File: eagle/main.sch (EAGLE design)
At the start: 32 parts, among them IC1 7805TV, U1 INA213AIDCKT, U2 LM1117MP-3.3, U3 INA213AIDCKT, U4 INA213AIDCKT, U5 S25FL064K0SMFI011

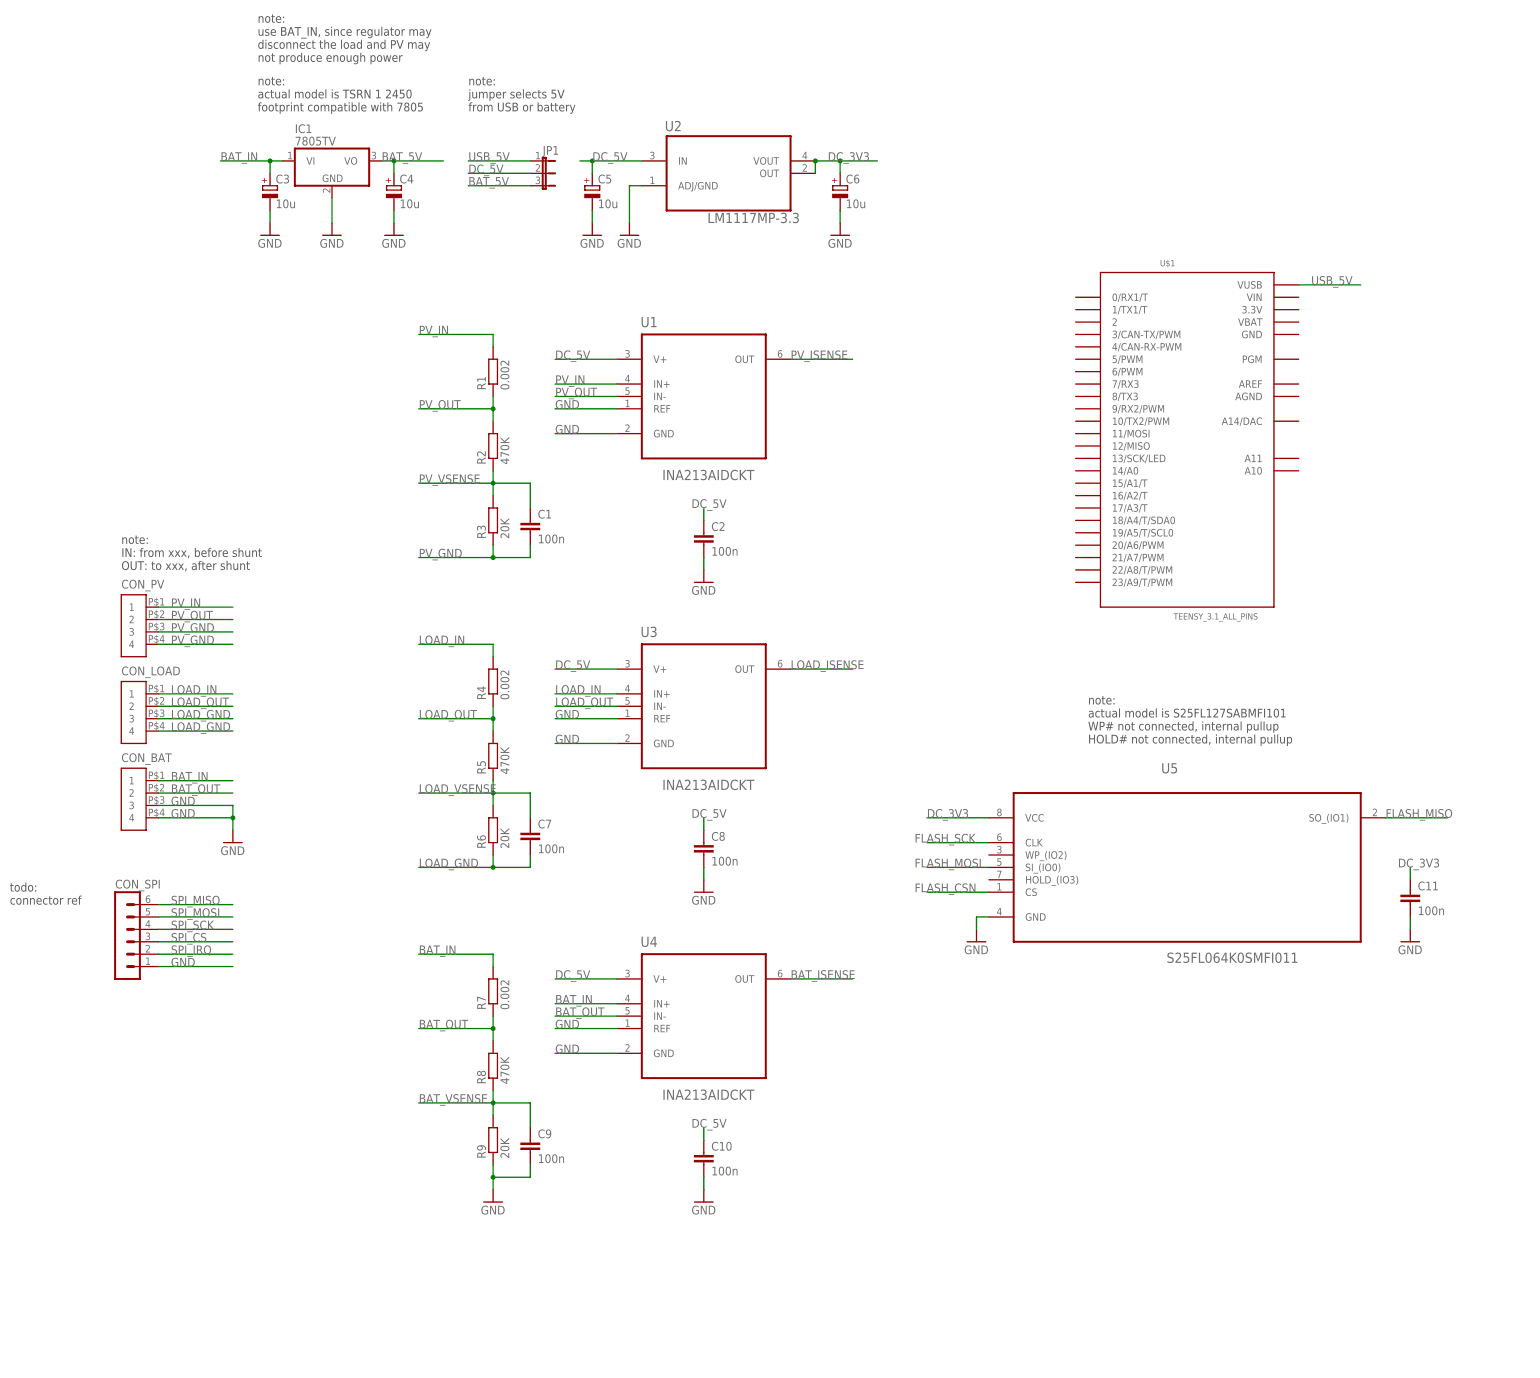
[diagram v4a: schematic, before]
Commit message: add TI library
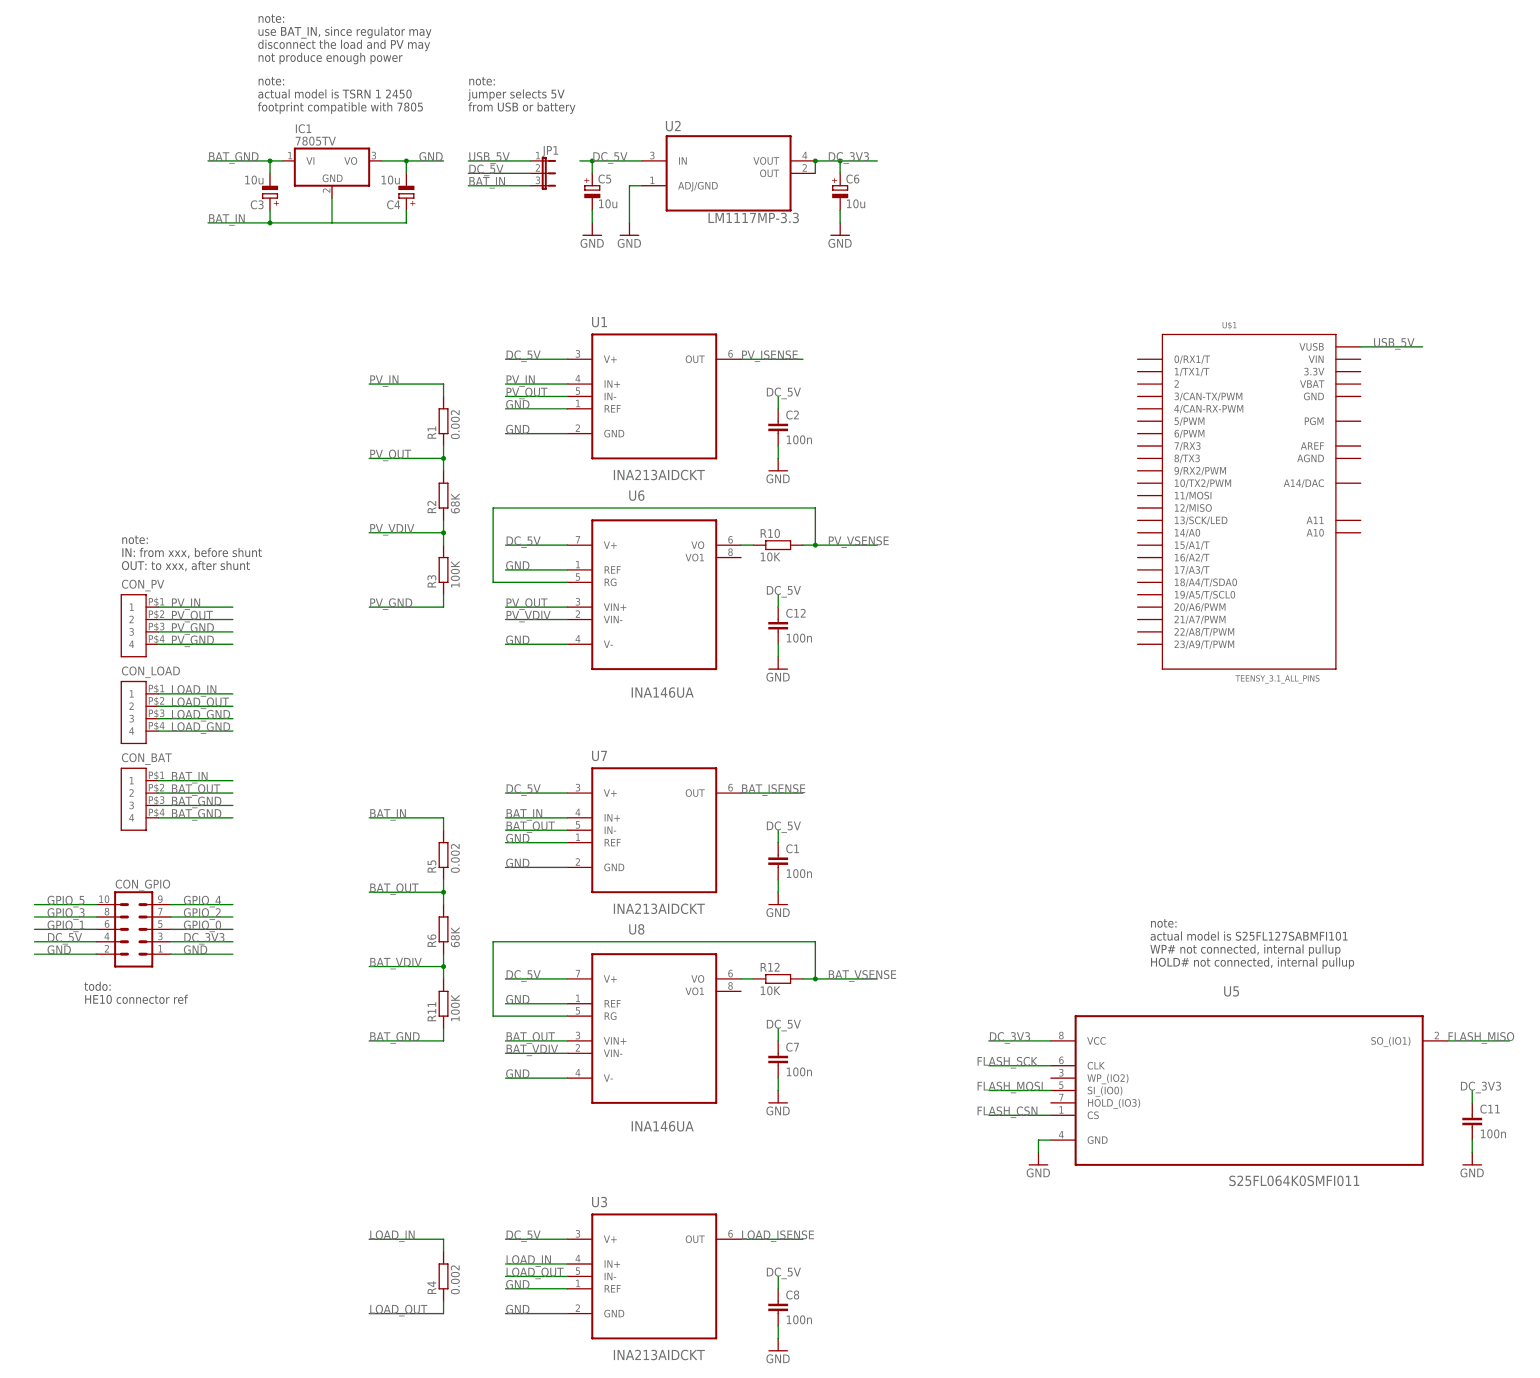
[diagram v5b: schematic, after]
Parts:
- removed C10, C9: 100n, rcl:C-EUC1206
- removed CON_SPI: (no value), con-lstb:MA06-1
- removed R7: 0.002, resistor:R-EU_R2512
- removed R8: 470K, rcl:R-EU_R0603
- removed R9: 20K, rcl:R-EU_R0603
- removed U4: INA213AIDCKT, TI-INA213AIDCKT:INA213AIDCKT
- added C12: 100n, rcl:C-EUC1206
- added CON_GPIO: (no value), con-lstb:MA05-2
- added R10, R12: 10K, rcl:R-EU_R0603
- added R11: 100K, rcl:R-EU_R0603
- added U6, U8: INA146UA, Texas Instruments_By_element14_Batch_1:INA146UA
- added U7: INA213AIDCKT, TI-INA213AIDCKT:INA213AIDCKT
- R2: value 470K -> 68K
- R3: value 20K -> 100K
- R5: value 470K -> 0.002; device rcl:R-EU_R0603 -> resistor:R-EU_R2512
- R6: value 20K -> 68K
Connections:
- removed net BAT_5V: C4.+, IC1.VO, JP1.3
- removed net LOAD_VSENSE: C7.1, R5.1, R6.2
- removed net SPI_CS: CON_SPI.3
- removed net SPI_IRQ: CON_SPI.2
- removed net SPI_MISO: CON_SPI.6
- removed net SPI_MOSI: CON_SPI.5
- removed net SPI_SCK: CON_SPI.4
- new net BAT_GND: C3.-, CON_BAT.3, CON_BAT.4, IC1.VI, R11.1
- new net BAT_VDIV: R11.2, R6.1, U8.VIN-
- new net GPIO_0: CON_GPIO.5
- new net GPIO_1: CON_GPIO.6
- new net GPIO_2: CON_GPIO.7
- new net GPIO_3: CON_GPIO.8
- new net GPIO_4: CON_GPIO.9
- new net GPIO_5: CON_GPIO.10
- new net N$1: R12.1, U8.VO
- new net N$2: R10.1, U6.VO
- new net N$4: IC1.GND
- new net PV_VDIV: R2.1, R3.2, U6.VIN-
- net BAT_IN: now also C4.+, JP1.3, R5.2, U7.IN+; no longer IC1.VI, R7.2, U4.IN+
- net BAT_ISENSE: now also U7.OUT; no longer U4.OUT
- net BAT_OUT: now also R5.1, R6.2, U7.IN-, U8.VIN+; no longer R7.1, R8.2, U4.IN-
- net BAT_VSENSE: now also R12.2, U8.RG; no longer C9.1, R8.1, R9.2
- net DC_3V3: now also CON_GPIO.3
- net DC_5V: now also C1.1, C12.1, C7.1, CON_GPIO.4, U6.V+, U7.V+, U8.V+; no longer C10.1, U4.V+
- net GND: now also C1.2, C12.2, C7.2, CON_GPIO.1, CON_GPIO.2, IC1.VO, U6.REF, U6.V-, U7.GND, U7.REF, U8.REF, U8.V-; no longer C10.2, C3.-, C9.2, CON_BAT.3, CON_BAT.4, CON_SPI.1, IC1.GND, R9.1, U4.GND, U4.REF
- net LOAD_GND: no longer C7.2, R6.1
- net LOAD_OUT: no longer R5.2
- net PV_GND: no longer C1.2
- net PV_OUT: now also U6.VIN+
- net PV_VSENSE: now also R10.2, U6.RG; no longer C1.1, R2.1, R3.2
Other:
- note added: "todo: HE10 connector ref"
- note removed: "todo: connector ref"
- moved on the sheet: C1, C11, C2, C3, C4, C7, C8, R1, R2, R3, R4, R5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

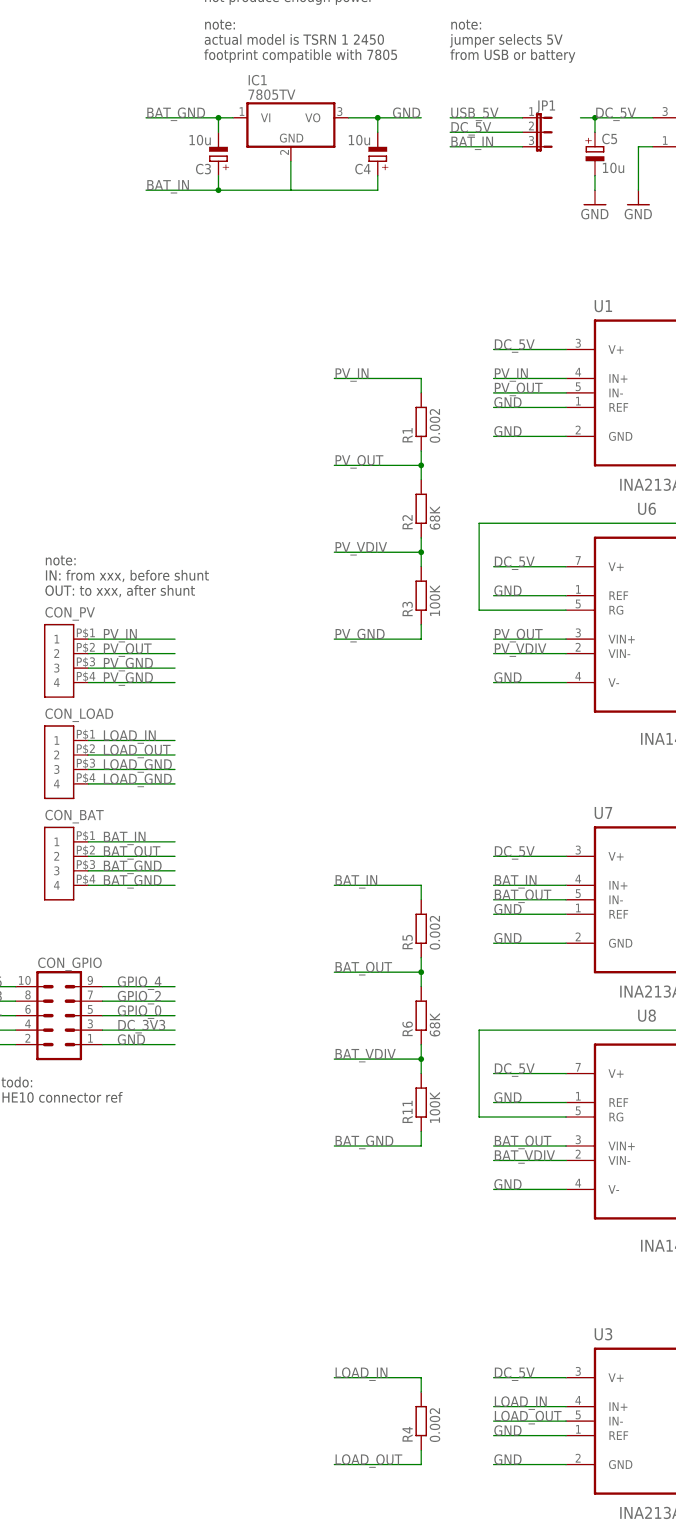
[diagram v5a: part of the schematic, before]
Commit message: rename PV, BAT, LOAD signals
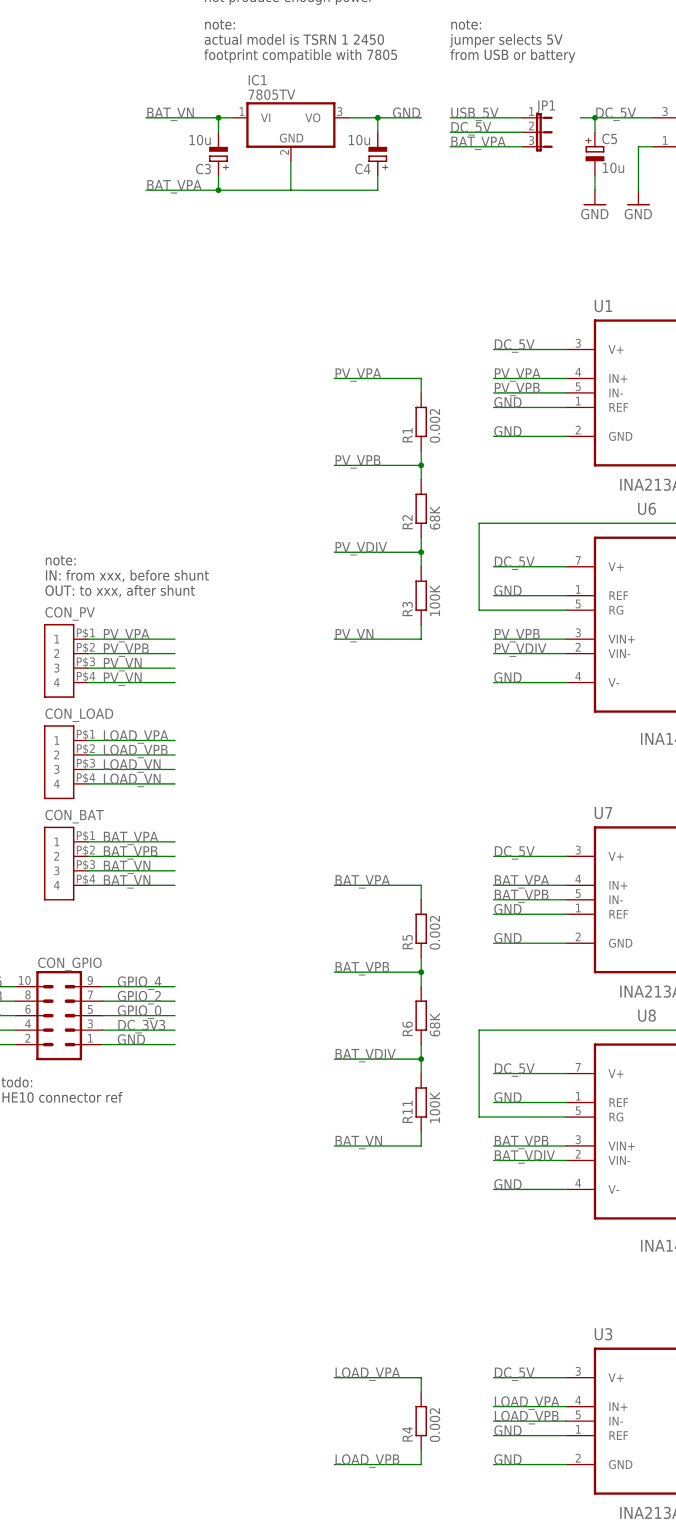
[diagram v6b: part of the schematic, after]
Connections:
- net BAT_GND renamed BAT_VN
- net BAT_IN renamed BAT_VPA
- net BAT_OUT renamed BAT_VPB
- net LOAD_GND renamed LOAD_VN
- net LOAD_IN renamed LOAD_VPA
- net LOAD_OUT renamed LOAD_VPB
- net PV_GND renamed PV_VN
- net PV_IN renamed PV_VPA
- net PV_OUT renamed PV_VPB
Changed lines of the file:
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@@
 </segment>
 </net>
-<net name="PV_IN" class="0">
+<net name="PV_VPA" class="0">
 <segment>
 <wire x1="0" y1="160.02" x2="15.24" y2="160.02" width="0.1524" layer="91"/>
@@
 </segment>
 </net>
-<net name="PV_OUT" class="0">
-<segment>
-<wire x1="0" y1="157.48" x2="15.24" y2="157.48" width="0.1524" layer="91"/>
-<label x="2.54" y="157.48" size="1.778" layer="95"/>
-<pinref part="CON_PV" gate="G$1" pin="2"/>
-</segment>
-<segment>
-<pinref part="U1" gate="A" pin="IN-"/>
-<wire x1="83.82" y1="203.2" x2="71.12" y2="203.2" width="0.1524" layer="91"/>
-<label x="71.12" y="203.2" size="1.778" layer="95"/>
-</segment>
-<segment>
-<pinref part="R1" gate="G$1" pin="1"/>
-<wire x1="58.42" y1="193.04" x2="58.42" y2="190.5" width="0.1524" layer="91"/>
-<label x="43.18" y="190.5" size="1.778" layer="95"/>
-<pinref part="R2" gate="G$1" pin="2"/>
-<wire x1="58.42" y1="190.5" x2="43.18" y2="190.5" width="0.1524" layer="91"/>
-<wire x1="58.42" y1="187.96" x2="58.42" y2="190.5" width="0.1524" layer="91"/>
-<junction x="58.42" y="190.5"/>
-</segment>
-<segment>
-<pinref part="U6" gate="A" pin="VIN+"/>
-<wire x1="83.82" y1="160.02" x2="71.12" y2="160.02" width="0.1524" layer="91"/>
-<label x="71.12" y="160.02" size="1.778" layer="95"/>
-</segment>
-</net>
-<net name="LOAD_IN" class="0">
+<net name="LOAD_VPA" class="0">
 <segment>
 <wire x1="0" y1="142.24" x2="15.24" y2="142.24" width="0.1524" layer="91"/>
@@
 </segment>
 </net>
-<net name="LOAD_OUT" class="0">
-<segment>
-<wire x1="0" y1="139.7" x2="15.24" y2="139.7" width="0.1524" layer="91"/>
-<label x="2.54" y="139.7" size="1.778" layer="95"/>
-<pinref part="CON_LOAD" gate="G$1" pin="2"/>
-</segment>
-<segment>
-<pinref part="R4" gate="G$1" pin="1"/>
-<wire x1="58.42" y1="17.78" x2="58.42" y2="15.24" width="0.1524" layer="91"/>
-<label x="43.18" y="15.24" size="1.778" layer="95"/>
-<wire x1="58.42" y1="15.24" x2="43.18" y2="15.24" width="0.1524" layer="91"/>
-</segment>
-<segment>
-<pinref part="U3" gate="A" pin="IN-"/>
-<wire x1="83.82" y1="22.86" x2="71.12" y2="22.86" width="0.1524" layer="91"/>
-<label x="71.12" y="22.86" size="1.778" layer="95"/>
-</segment>
-</net>
-<net name="BAT_IN" class="0">
+<net name="BAT_VPA" class="0">
 <segment>
 <wire x1="0" y1="124.46" x2="15.24" y2="124.46" width="0.1524" layer="91"/>
@@
 </segment>
 </net>
-<net name="BAT_OUT" class="0">
+<net name="BAT_VPB" class="0">
 <segment>
 <wire x1="0" y1="121.92" x2="15.24" y2="121.92" width="0.1524" layer="91"/>
@@
 </segment>
 </net>
-<net name="LOAD_GND" class="0">
+<net name="LOAD_VN" class="0">
 <segment>
 <wire x1="0" y1="137.16" x2="15.24" y2="137.16" width="0.1524" layer="91"/>
@@
 </segment>
 </net>
-<net name="PV_GND" class="0">
+<net name="PV_VN" class="0">
 <segment>
 <wire x1="0" y1="154.94" x2="15.24" y2="154.94" width="0.1524" layer="91"/>
@@
 </segment>
 </net>
-<net name="BAT_GND" class="0">
+<net name="BAT_VN" class="0">
 <segment>
 <wire x1="0" y1="119.38" x2="15.24" y2="119.38" width="0.1524" layer="91"/>
@@
 </segment>
 </net>
+<net name="PV_VPB" class="0">
+<segment>
+<wire x1="0" y1="157.48" x2="15.24" y2="157.48" width="0.1524" layer="91"/>
+<label x="2.54" y="157.48" size="1.778" layer="95"/>
+<pinref part="CON_PV" gate="G$1" pin="2"/>
+</segment>
+<segment>
+<pinref part="U1" gate="A" pin="IN-"/>
+<wire x1="83.82" y1="203.2" x2="71.12" y2="203.2" width="0.1524" layer="91"/>
+<label x="71.12" y="203.2" size="1.778" layer="95"/>
+</segment>
+<segment>
+<pinref part="R1" gate="G$1" pin="1"/>
+<wire x1="58.42" y1="193.04" x2="58.42" y2="190.5" width="0.1524" layer="91"/>
+<label x="43.18" y="190.5" size="1.778" layer="95"/>
+<pinref part="R2" gate="G$1" pin="2"/>
+<wire x1="58.42" y1="190.5" x2="43.18" y2="190.5" width="0.1524" layer="91"/>
+<wire x1="58.42" y1="187.96" x2="58.42" y2="190.5" width="0.1524" layer="91"/>
+<junction x="58.42" y="190.5"/>
+</segment>
+<segment>
+<pinref part="U6" gate="A" pin="VIN+"/>
+<wire x1="83.82" y1="160.02" x2="71.12" y2="160.02" width="0.1524" layer="91"/>
+<label x="71.12" y="160.02" size="1.778" layer="95"/>
+</segment>
+</net>
+<net name="LOAD_VPB" class="0">
+<segment>
+<wire x1="0" y1="139.7" x2="15.24" y2="139.7" width="0.1524" layer="91"/>
+<label x="2.54" y="139.7" size="1.778" layer="95"/>
+<pinref part="CON_LOAD" gate="G$1" pin="2"/>
+</segment>
+<segment>
+<pinref part="R4" gate="G$1" pin="1"/>
+<wire x1="58.42" y1="17.78" x2="58.42" y2="15.24" width="0.1524" layer="91"/>
+<label x="43.18" y="15.24" size="1.778" layer="95"/>
+<wire x1="58.42" y1="15.24" x2="43.18" y2="15.24" width="0.1524" layer="91"/>
+</segment>
+<segment>
+<pinref part="U3" gate="A" pin="IN-"/>
+<wire x1="83.82" y1="22.86" x2="71.12" y2="22.86" width="0.1524" layer="91"/>
+<label x="71.12" y="22.86" size="1.778" layer="95"/>
+</segment>
+</net>
